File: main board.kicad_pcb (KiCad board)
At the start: 2 copper layers, 159 x 146 mm, 119 parts, among them J1 #15, J10 #11, J11 #14, J12 #37, J13 #3, J14 #23, J15 #33, J16 #38, J17 #4, J18 #13, J19 #9, J2 Red-Blk, J20 #18, J21 #22, J22 #21, J23 #25, J24 #8, J25 #16, J26 #12, J27 #35, J28 #7, J29 #19, J3 #2, J30 #26, J31 #5, J32 #28, J33 #32, J34 #39, J35 #27, J36 #40, J37 #17, J38 #20, J39 #24, J4 Blk, J40 #29, J41 #30, J42 #31, J43 #34, J44 #36, J45 #Brn, J46 #Blu, J47 #41, J48 LED conn, J49 #42 1.5V, J5 #1, J50 #6.3V, J51 #6.3V, J6 #6, J7 #10, J8 Red-Yel, J9 Red-Grn, Q1 2N2907, Q2 BD136, Q3 PN2222A, Q4 2N2907, U1 6AL5, U2 ECC83

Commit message: Improve layout
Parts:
- added R100: 1k, Resistor_THT:R_Axial_DIN0414_L11.9mm_D4.5mm_P5.08mm_Vertical, F.Cu at (154.4, 91.3)
- added REF**: OSHW-Logo2_24.3x20mm_SilkScreen, Symbol:OSHW-Logo2_24.3x20mm_SilkScreen, B.Cu at (172.2, 132.6)
- added REF**: OSHW-Logo2_24.3x20mm_SilkScreen, Symbol:OSHW-Logo2_24.3x20mm_SilkScreen, F.Cu at (172.2, 132.7)
- CR1: footprint Diode_THT:D_DO-41_SOD81_P5.08mm_Vertical_KathodeUp -> Diode_THT:D_DO-41_SOD81_P3.81mm_Vertical_AnodeUp
- H1: value MountingHole -> Earth
- TP5: value Lp -> L.Pl.
- TP6: value Rp -> R.Pl.
- moved R32 16.7 mm to (181.8, 105.7)
- moved TP3 6.95 mm to (162.8, 111.6)
- moved J13 4.90 mm to (159.5, 105.6)
- moved CR1 3.59 mm to (149.4, 92.1), turned to 90 degrees
- moved J8 0.70 mm to (147.8, 84.2)
- renumbered C9 to C100, C10 to C101, C11 to C102, R12 to R101, R9 to R102, R11 to R103, R13 to R104, R14 to R105
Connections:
- CR1 pad 1: Net-(C8-Pad1) -> Net-(CR1-Pad1)
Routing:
- net Net-(R32-Pad1): track 69.6 -> 53.2 mm, vias 3 -> 2
- net Net-(CR1-Pad1): track 0.00 -> 5.33 mm
- net Net-(CR1-Pad2): track 6.41 -> 4.05 mm
- net Net-(C8-Pad2): track 64.1 -> 62.5 mm
- net Net-(C8-Pad1): track 40.0 -> 41.0 mm
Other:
- board text added: "06.2020"
- board text added: "Rev. A"

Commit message: Fixes after Rev.A was assembled
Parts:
- removed the REF** at (172.2, 132.7)
- added TP8: TP-GND, TestPoint:TestPoint_THTPad_2.0x2.0mm_Drill1.0mm, F.Cu at (244.8, 150.7)
- added TP9: Pnt D, TestPoint:TestPoint_THTPad_2.0x2.0mm_Drill1.0mm, F.Cu at (134.9, 119.2)
- C100, C101: value 1000uF -> 2000uF
- TP1, TP2, TP3: moved to B.Cu
- moved J34 24.7 mm to (107.3, 130.2)
- moved TP1 4.51 mm to (207.9, 76.7)
- moved C101 1.24 mm to (171.6, 77.9)
- moved D1 0.32 mm to (126.8, 65.9)
- moved D2 0.30 mm to (122.9, 71.0)
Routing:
- net Net-(J34-Pad1): track 6.20 -> 21.7 mm
- net Net-(J17-Pad1): track 16.2 -> 21.3 mm
- net Net-(C102-Pad1): track 71.6 -> 68.9 mm
- net Net-(C100-Pad2): track 74.9 -> 73.2 mm
- net Net-(C8-Pad1): track 41.0 -> 41.5 mm
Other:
- board text added: "Rev. B"
- board text removed: "06.2020"
- board text removed: "Rev. A"

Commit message: Put back original resistors
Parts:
- removed R11.1: 15M, Resistor_THT:R_Axial_DIN0309_L9.0mm_D3.2mm_P5.08mm_Vertical
- removed R11.2: 1M, Resistor_THT:R_Axial_DIN0309_L9.0mm_D3.2mm_P5.08mm_Vertical
- removed R12.1: 2M, Resistor_THT:R_Axial_DIN0411_L9.9mm_D3.6mm_P7.62mm_Vertical
- removed R12.2: 5M, Resistor_THT:R_Axial_DIN0411_L9.9mm_D3.6mm_P7.62mm_Vertical
- removed R9.1: 8.45M, Resistor_THT:R_Axial_DIN0207_L6.3mm_D2.5mm_P5.08mm_Vertical
- removed R9.2: 40.2k, Resistor_THT:R_Axial_DIN0207_L6.3mm_D2.5mm_P5.08mm_Vertical
- added D6: 6V9, Diode_THT:D_DO-35_SOD27_P5.08mm_Vertical_KathodeUp, F.Cu at (186.2, 86.8)
- added J52: #23.1, wv98:Hole_Din1.2mm_Dout3mm, F.Cu at (188.2, 179.6)
- added R11: 16M, wv98:R2, F.Cu at (146.9, 123.5)
- added R12: 7M, wv98:R12, F.Cu at (164.2, 186.0)
- added R9: 8.49M, wv98:R1-like, F.Cu at (158.3, 132.9)
- R8: footprint Resistor_THT:R_Axial_DIN0207_L6.3mm_D2.5mm_P5.08mm_Vertical -> wv98:R1-like
- moved R10 47.6 mm to (208.4, 122.5)
- moved C100 27.8 mm to (171.4, 73.0)
- moved D3 23.9 mm to (179.8, 77.9), turned to 270 degrees
- moved D4 21.5 mm to (183.1, 83.1), turned to 90 degrees
- moved R30 21.2 mm to (118.4, 89.6)
- moved J48 21.1 mm to (213.4, 70.0), turned to 180 degrees
- moved J14 15.9 mm to (217.6, 187.2)
- moved RV1 12.7 mm to (231.7, 78.5), turned to 180 degrees
- moved TP9 12.3 mm to (146.9, 116.4)
- moved R8 11.7 mm to (181.3, 176.5)
- moved R101 10.7 mm to (209.6, 75.1), turned to 90 degrees
- moved J51 10.1 mm to (186.0, 133.7)
- moved J17 9.48 mm to (146.9, 130.8)
- moved J35 8.24 mm to (204.5, 129.0)
- moved J31 8.10 mm to (197.3, 128.9)
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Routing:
- net Net-(R10-Pad1): track 86.6 -> 17.9 mm, vias 2 -> 0
- net Net-(J17-Pad1): track 21.3 -> 67.8 mm
- net Net-(C100-Pad1): track 75.9 -> 100.3 mm
- net Net-(D4-Pad1): track 33.3 -> 15.6 mm
- net Net-(C8-Pad2): track 62.5 -> 77.2 mm
- net Net-(Q4-Pad3): track 23.8 -> 10.8 mm
- net Net-(J18-Pad1): track 59.7 -> 47.2 mm
- net Net-(J15-Pad1): track 83.9 -> 71.3 mm
- net Net-(J35-Pad1): track 6.00 -> 14.8 mm
- net Net-(R32-Pad1): track 53.2 -> 45.3 mm, vias 2 -> 0
- net Net-(R12.1-Pad2): track 5.88 -> 0.00 mm
- net Net-(J29-Pad1): track 27.6 -> 22.0 mm
- net Net-(R28-Pad2): track 13.9 -> 18.8 mm
- net Net-(R9.1-Pad1): track 4.83 -> 0.00 mm
- net Net-(Q2-Pad3): track 17.9 -> 13.4 mm
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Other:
- board text added: "+"
- board text added: "0.5 DC"
- board text removed: "0.5VDC"

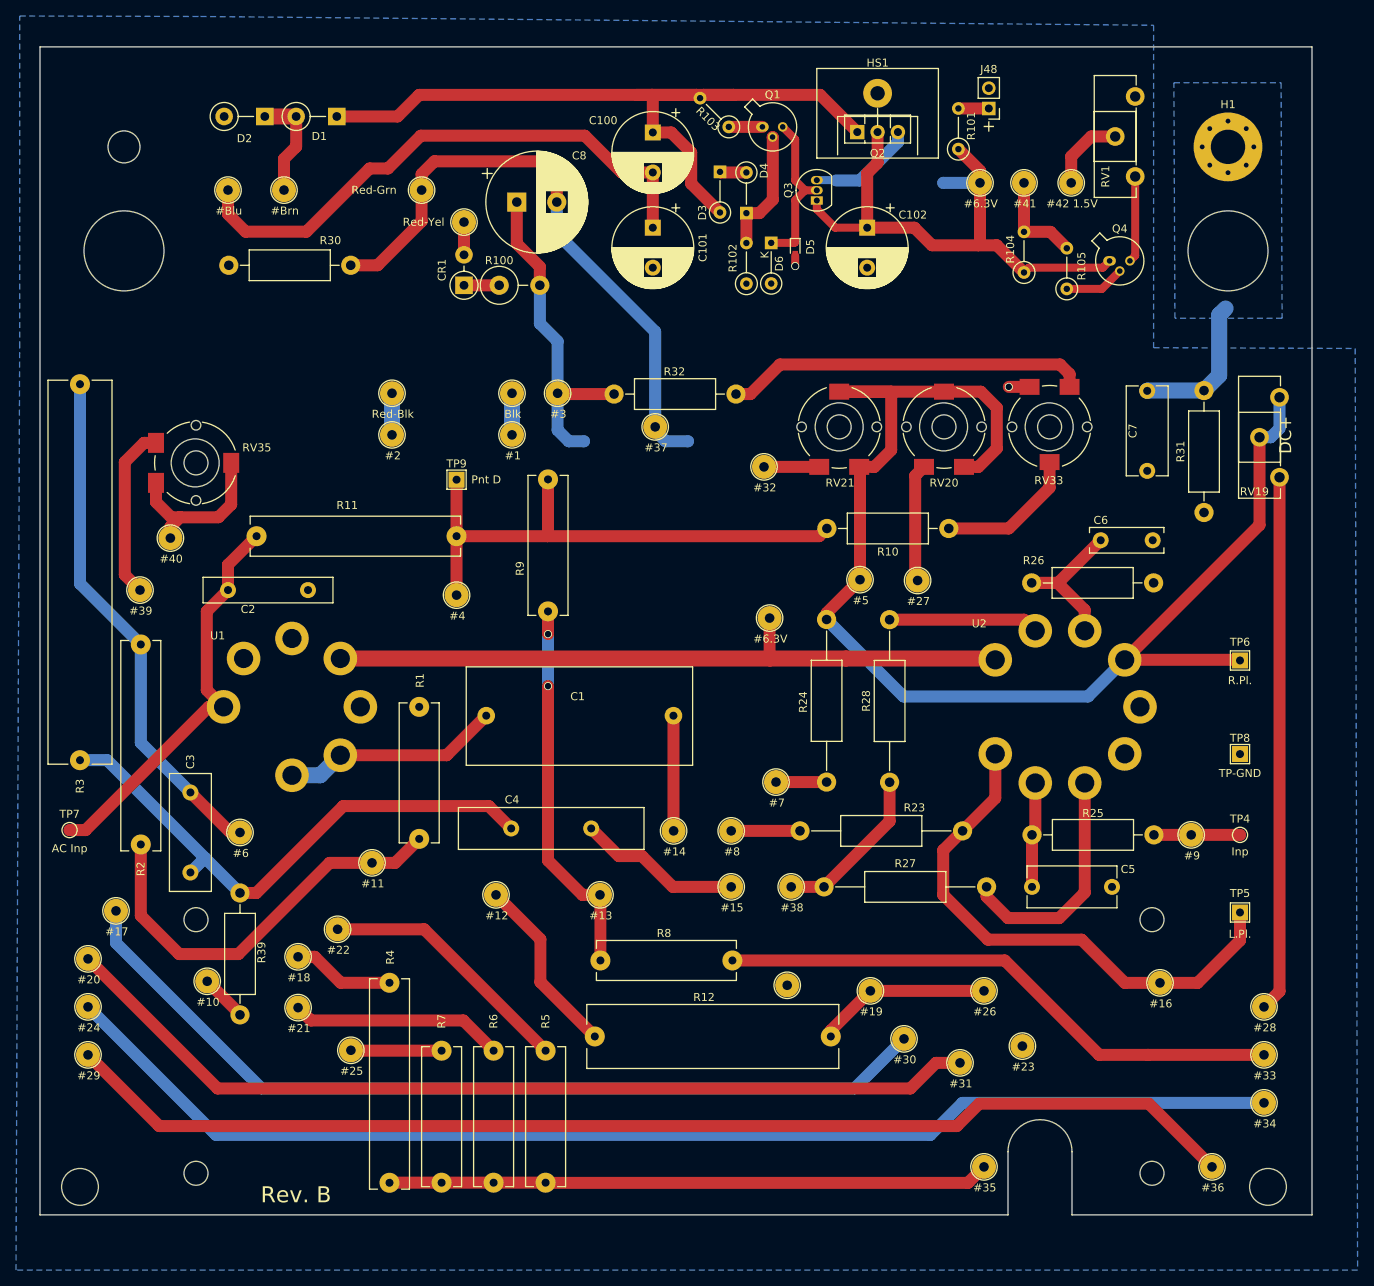
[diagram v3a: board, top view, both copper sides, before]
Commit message: Remove 6AL5 and replace it with diodes
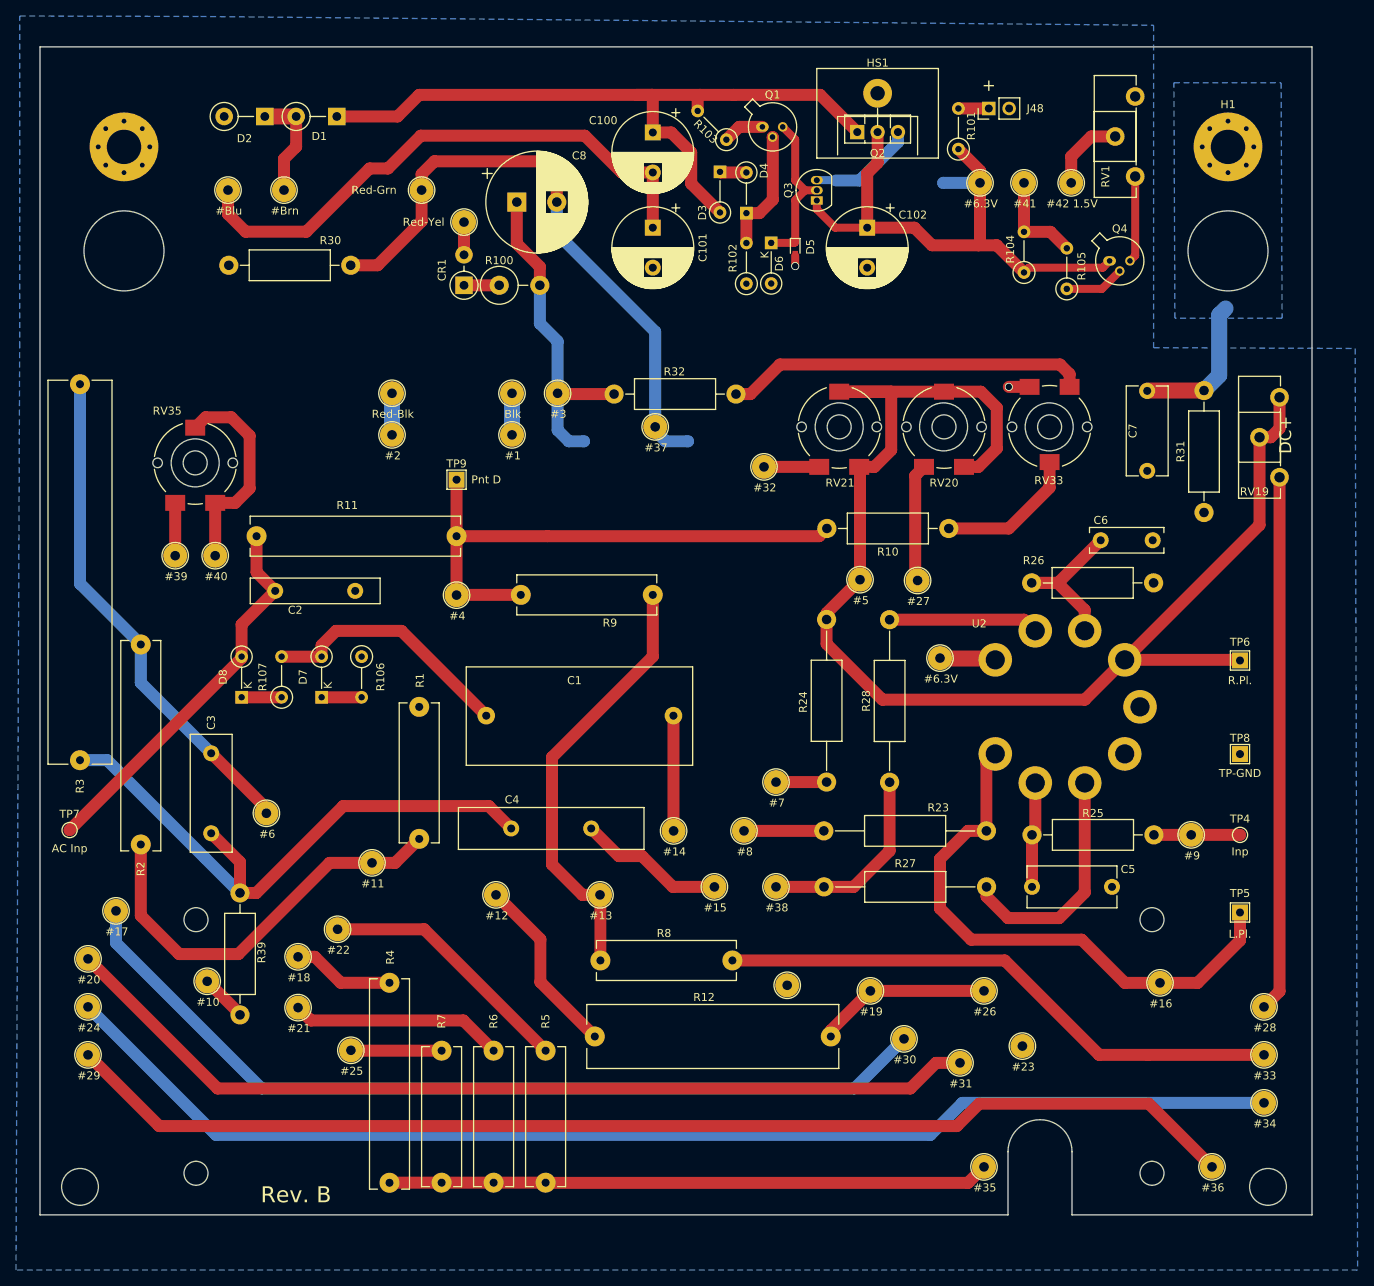
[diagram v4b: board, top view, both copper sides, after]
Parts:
- removed U1: 6AL5, wv98:6AL5
- added ?: , MountingHole:MountingHole_4.3mm_M4_Pad_Via, F.Cu at (105.3, 74.8)
- added D7: 1N4148, Diode_THT:D_DO-35_SOD27_P5.08mm_Vertical_KathodeUp, F.Cu at (130.0, 143.6)
- added D8: 1N4148, Diode_THT:D_DO-35_SOD27_P5.08mm_Vertical_KathodeUp, F.Cu at (120.0, 143.6)
- added R106: 180, Resistor_THT:R_Axial_DIN0207_L6.3mm_D2.5mm_P5.08mm_Vertical, F.Cu at (135.0, 138.5)
- added R107: 180, Resistor_THT:R_Axial_DIN0207_L6.3mm_D2.5mm_P5.08mm_Vertical, F.Cu at (125.0, 143.6)
- moved J51 21.9 mm to (207.3, 138.7)
- moved R9 13.3 mm to (171.4, 130.8), turned to 180 degrees
- moved J34 6.15 mm to (111.7, 125.9)
- moved J36 6.02 mm to (116.7, 125.9)
- moved C2 5.90 mm to (124.2, 130.3)
- moved C3 5.55 mm to (116.2, 150.6)
- moved J6 4.08 mm to (123.1, 158.1)
- moved R23 2.98 mm to (213.1, 160.3)
- moved J1 2.10 mm to (179.1, 167.3)
- moved J16 1.90 mm to (186.8, 167.3)
- moved R103 1.63 mm to (180.6, 73.9)
- moved J24 1.60 mm to (182.8, 160.3)
- moved REF** 0.85 mm to (171.4, 132.3)
- moved RV35 0.36 mm to (114.2, 114.6), turned to 0 degrees
- turned J48 to 90 degrees
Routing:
- net Net-(J51-Pad1): track 87.0 -> 7.00 mm
- net Net-(J34-Pad1): track 21.7 -> 6.60 mm
- net Net-(C100-Pad1): track 100.3 -> 91.8 mm
- net Net-(J18-Pad1): track 47.2 -> 54.7 mm, vias 2 -> 0
- net Net-(C3-Pad2): track 69.0 -> 75.4 mm
- net Net-(D8-Pad1): track 0.00 -> 5.00 mm
- net Net-(D7-Pad1): track 0.00 -> 5.00 mm
- net Net-(J36-Pad1): track 21.5 -> 26.5 mm
- net Net-(C1-Pad2): track 27.4 -> 32.1 mm
- net Net-(J16-Pad1): track 20.6 -> 24.6 mm
- net Net-(J25-Pad1): track 67.7 -> 70.6 mm
- net Net-(J31-Pad1): track 169.5 -> 171.6 mm
- net Net-(C4-Pad2): track 20.5 -> 18.4 mm
- net Net-(C2-Pad1): track 50.4 -> 48.3 mm
- net Net-(C3-Pad1): track 65.0 -> 63.3 mm
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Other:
- outline, holes or cut-outs redrawn
